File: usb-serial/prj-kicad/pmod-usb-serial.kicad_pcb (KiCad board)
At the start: 2 copper layers, 38.1 x 20.3 mm, 18 parts, among them P1 PMOD, P2 CONN_MiniUSB-AB, U1 CP2104

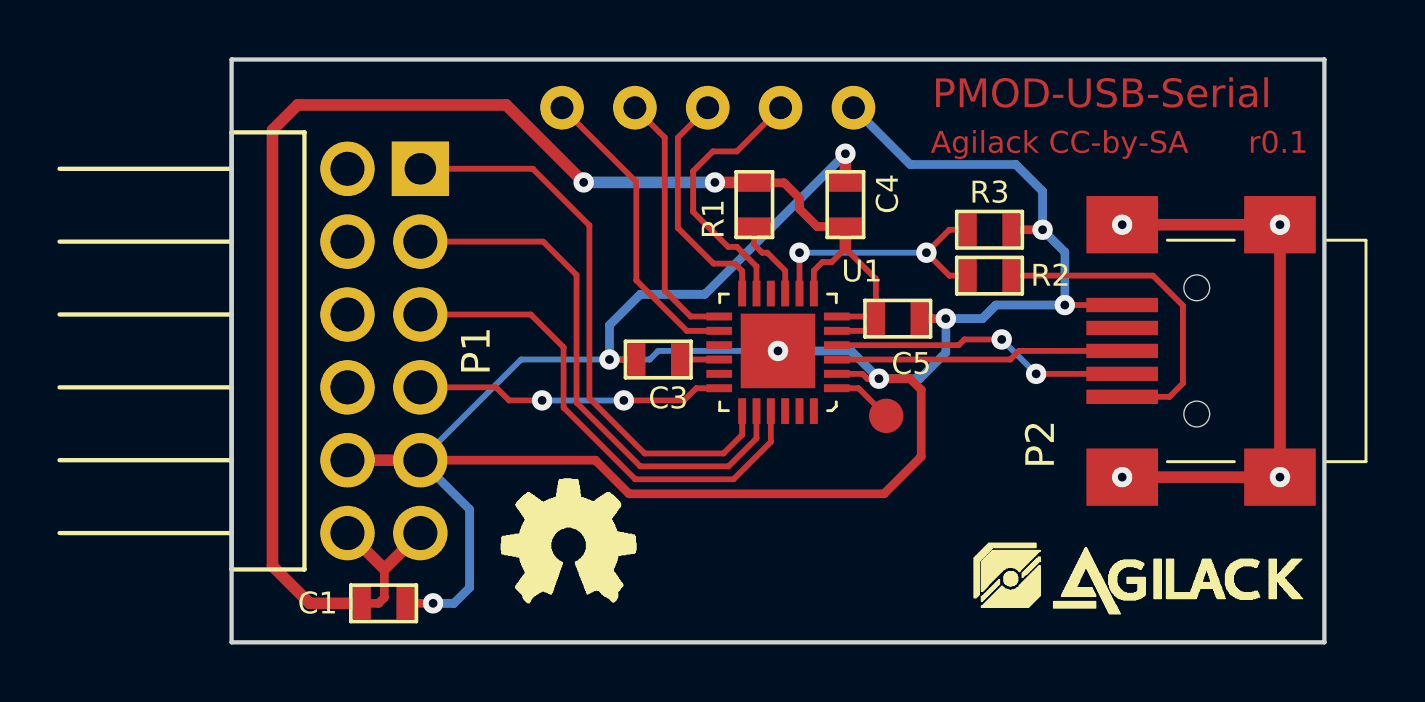
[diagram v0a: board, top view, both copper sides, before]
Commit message: added txs0104
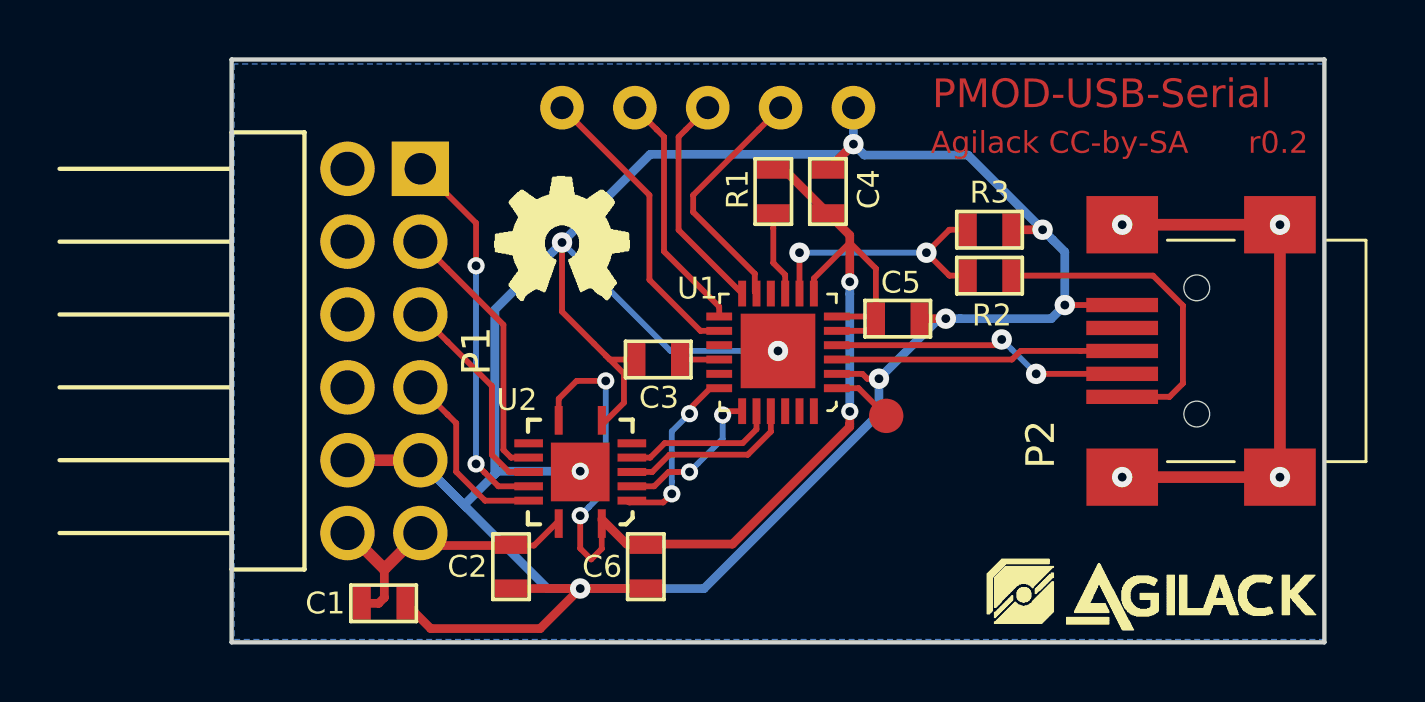
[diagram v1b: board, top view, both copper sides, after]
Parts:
- added C2: 100nF, pmod-usb-serial:SMD0603, F.Cu at (132.8, 112.5)
- added C6: 100nF, pmod-usb-serial:SMD0603, F.Cu at (137.5, 112.5)
- added U2: TXS0104, pmod-usb-serial:QFN14, F.Cu at (135.3, 109.2)
- moved logo_ohw 10.5 mm to (134.6, 101.2)
- moved R1 0.80 mm to (142.0, 99.4)
- moved C4 0.76 mm to (143.9, 99.4)
- moved agilack-11.5 0.72 mm to (155.6, 113.5)
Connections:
- C4 pad 1: VCC -> VCC_3V3
- C5 pad 1: VCC -> VCC_3V3
- R1 pad 1: VCC -> VCC_3V3
- U1 pad 18: PMOD_RTS -> CP21_CTS
- U1 pad 19: PMOD_CTS -> CP21_RTS
- U1 pad 20: PMOD_TXD -> CP21_RXD
- U1 pad 21: PMOD_RXD -> CP21_TXD
- U1 pad 5: VCC -> VCC_3V3
- U1 pad 6: VCC -> VCC_3V3
- U1 pad 7: VCC -> VCC_3V3
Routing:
- net VCC: track 55.5 -> 10.9 mm, vias 2 -> 0
- net VCC_3V3: track 0.00 -> 40.7 mm, vias 0 -> 4
- net GND: track 90.3 -> 108.0 mm, vias 8 -> 9
- net PMOD_RXD: track 17.4 -> 7.70 mm
- net PMOD_TXD: track 18.9 -> 9.70 mm
- net PMOD_CTS: track 20.0 -> 13.5 mm, vias 0 -> 2
- net CP21_TXD: track 0.00 -> 6.39 mm
- net CP21_CTS: track 0.00 -> 6.24 mm, vias 0 -> 2
- net CP21_RTS: track 0.00 -> 5.67 mm, vias 0 -> 2
- net CP21_RXD: track 0.00 -> 5.64 mm
- net PMOD_RTS: track 10.8 -> 6.55 mm, vias 2 -> 0
- net Net-(TP4-Pad1): track 9.33 -> 8.66 mm
- net Net-(TP2-Pad1): track 9.08 -> 8.50 mm
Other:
- board text added: "r0.2"
- board text removed: "r0.1"

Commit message: pmod-usb-serial wait for validation
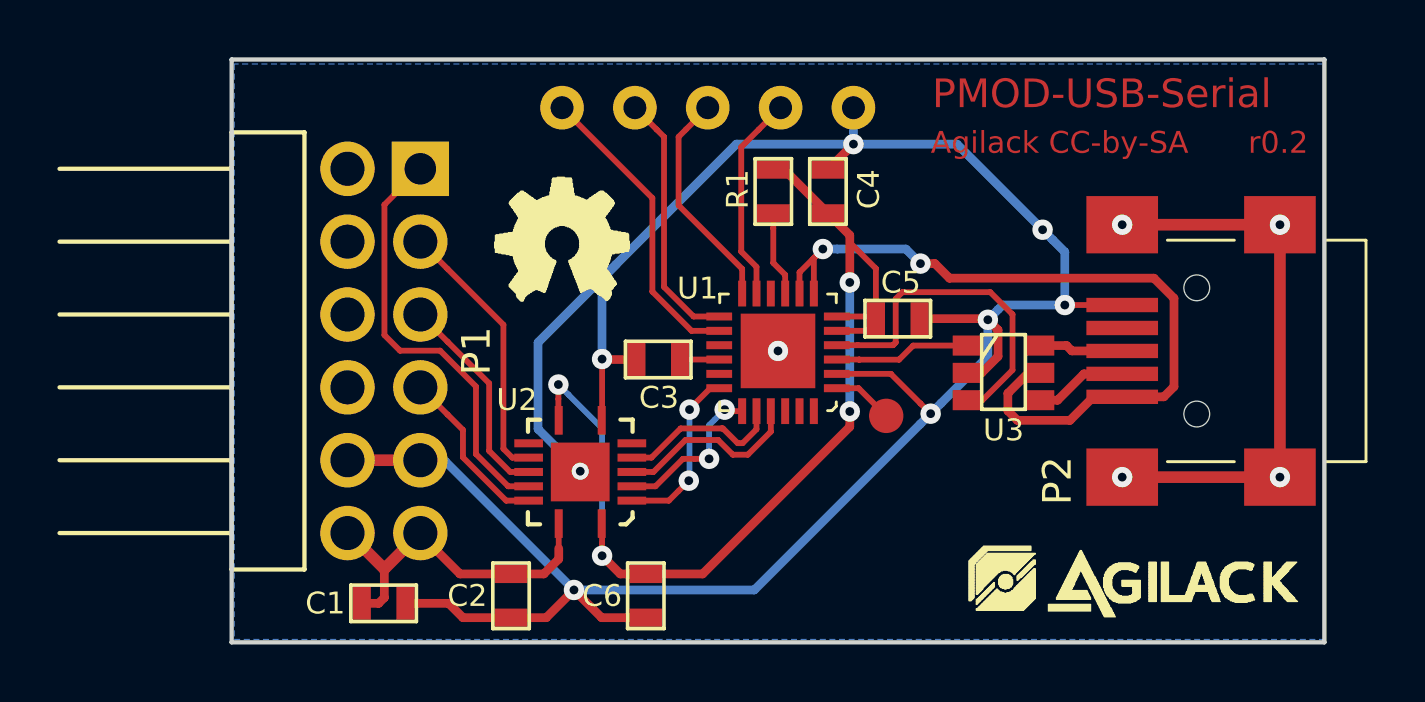
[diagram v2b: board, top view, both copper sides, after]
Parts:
- removed R2, R3: R, pmod-usb-serial:SMD0603
- added U3: USBLC6-2, pmod-usb-serial:SOT23-6, F.Cu at (150.0, 105.8)
- moved C2 1.02 mm to (132.8, 113.5)
- moved C6 1.02 mm to (137.5, 113.5)
- moved agilack-11.5 0.78 mm to (154.9, 113.1)
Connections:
- U1 pad 3: Net-(P2-Pad3) -> Net-(U1-Pad3)
- U1 pad 4: Net-(P2-Pad2) -> Net-(U1-Pad4)
- U1 pad 7: VCC_3V3 -> Net-(P2-Pad1)
- U1 pad 8: Net-(R2-Pad1) -> Net-(P2-Pad1)
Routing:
- net Net-(P2-Pad1): track 11.4 -> 28.0 mm, vias 0 -> 2
- net GND: track 108.0 -> 91.9 mm
- net Net-(U1-Pad4): track 0.00 -> 12.1 mm
- net Net-(R2-Pad1): track 9.39 -> 0.00 mm, vias 2 -> 0
- net Net-(P2-Pad2): track 10.5 -> 3.25 mm, vias 2 -> 0
- net Net-(P2-Pad3): track 10.1 -> 2.95 mm
- net Net-(U1-Pad3): track 0.00 -> 4.75 mm
- net VCC_3V3: track 40.7 -> 36.9 mm
- net PMOD_CTS: track 13.5 -> 15.6 mm, vias 2 -> 1
- net VCC: track 10.9 -> 12.7 mm
- net Net-(TP4-Pad1): track 8.66 -> 7.27 mm
- net Net-(TP2-Pad1): track 8.50 -> 9.02 mm
